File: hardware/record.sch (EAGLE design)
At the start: 24 parts, among them U1 MAX9939, U2 CBRHDSH1-40L, U3 MSP430FR5728_RGE_24, U4 FDG6303N, U5 FDG6303N

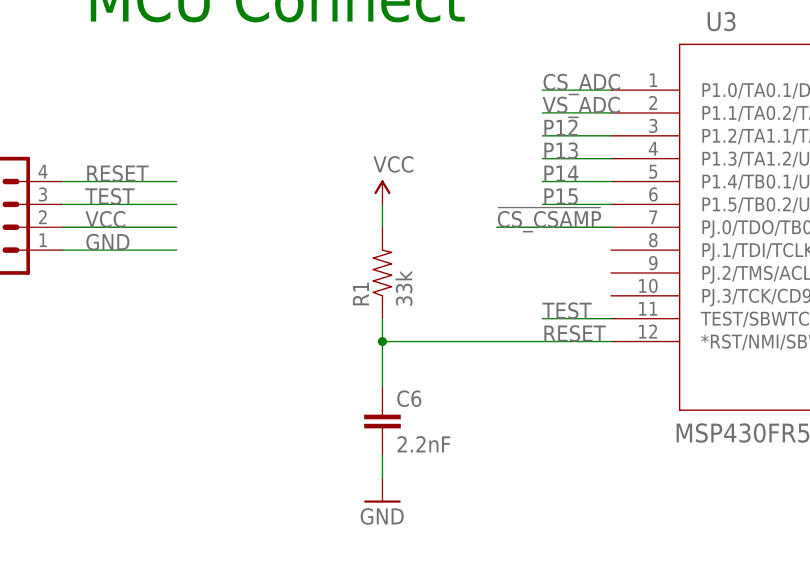
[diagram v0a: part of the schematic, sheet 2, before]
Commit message: Final demo for California. Everything works well. Four nodes stress test worked great. Not awesome with quick changing energy harvesters like piezo though.
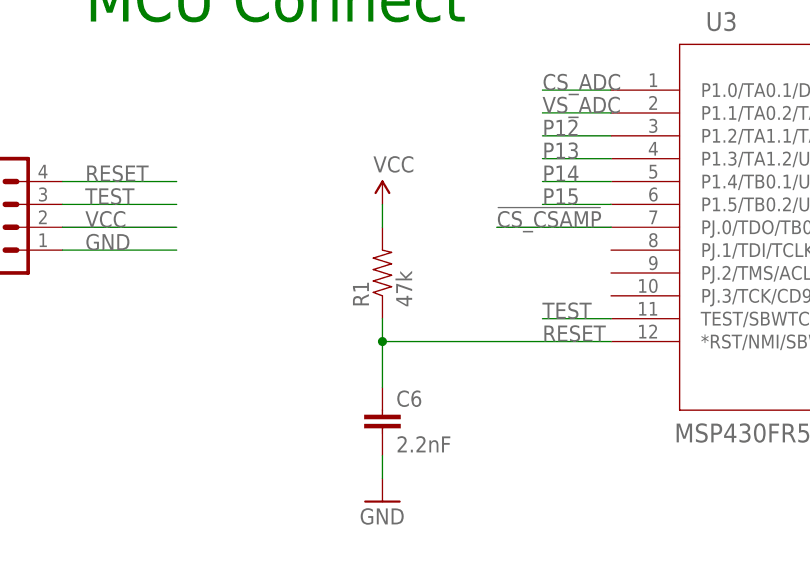
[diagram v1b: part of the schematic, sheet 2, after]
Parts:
- R1: value 33k -> 47k
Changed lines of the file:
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@@
 <part name="C6" library="SparkFun-Capacitors" deviceset="1UF-25V-10%(0805)" device="" value="2.2nF"/>
 <part name="GND14" library="SparkFun-Aesthetics" deviceset="GND" device=""/>
-<part name="R1" library="SparkFun-Resistors" deviceset="0.22OHM1/4W1%(0805)" device="" value="33k"/>
+<part name="R1" library="SparkFun-Resistors" deviceset="0.22OHM1/4W1%(0805)" device="" value="47k"/>
 <part name="SUPPLY1" library="SparkFun-Aesthetics" deviceset="VCC" device=""/>
 <part name="JP2" library="SparkFun-Connectors" deviceset="M04" device="PTH"/>
